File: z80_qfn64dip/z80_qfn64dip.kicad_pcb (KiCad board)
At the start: 2 copper layers, 62.8 x 23 mm, 28 parts, among them U1 Caravel_QFN, U2 Z80CPU, U3 AZ1117-3.3, U4 AP2112K-1.8, X1 10MHz

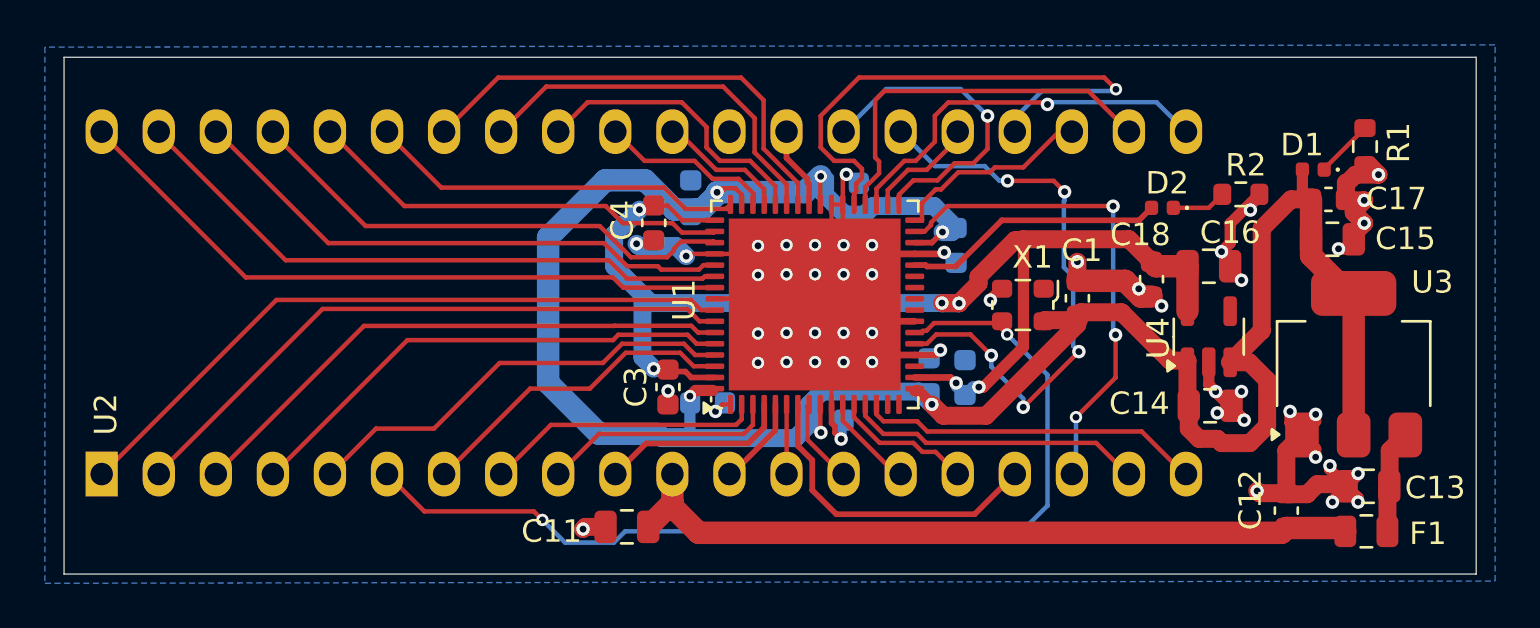
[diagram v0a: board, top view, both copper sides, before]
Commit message: add flash and move to 4 layers
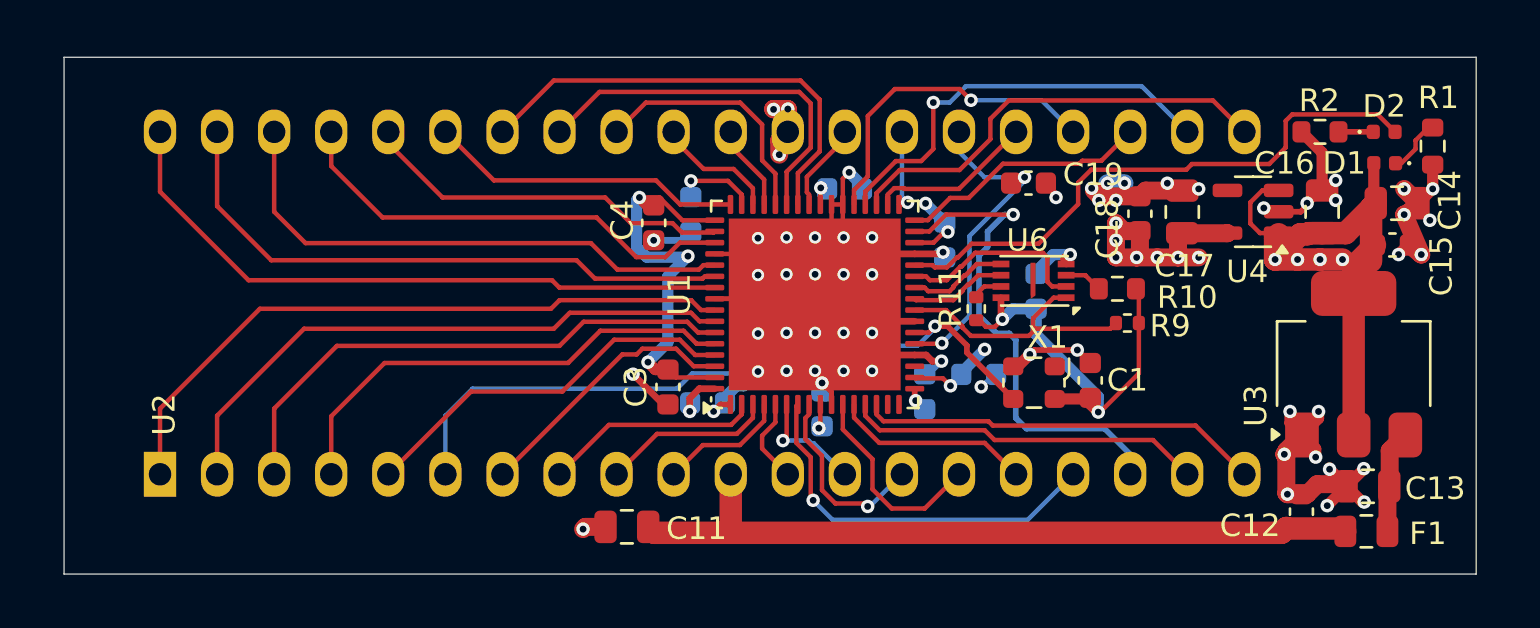
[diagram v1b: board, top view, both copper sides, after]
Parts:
- added C19: 1uF, Capacitor_SMD:C_0603_1608Metric, F.Cu at (157.5, 78.1)
- added C20: 100nF, Capacitor_SMD:C_0603_1608Metric, B.Cu at (157.9, 82.9)
- added R10: 10k, Resistor_SMD:R_0603_1608Metric, F.Cu at (161.5, 82.8)
- added R11: 10k, Resistor_SMD:R_0402_1005Metric, F.Cu at (155.2, 83.7)
- added R9: 10k, Resistor_SMD:R_0402_1005Metric, F.Cu at (161.9, 84.3)
- added U6: AT25EU0081A, KiCadModels:UDFN-8-1EP-2x3mm_P0.5mm_EP1.6x0.2mm, F.Cu at (157.7, 82.5)
- C14: value 10uF -> 22uF
- C15: value 22uF -> 100nF; footprint Capacitor_SMD:C_0805_2012Metric -> Capacitor_SMD:C_0603_1608Metric
- C17: value 100nF -> 10uF; footprint Capacitor_SMD:C_0603_1608Metric -> Capacitor_SMD:C_0805_2012Metric
- moved C14 12.3 mm to (173.9, 79.0)
- moved D2 10.4 mm to (173.4, 75.8), turned to 0 degrees
- moved C17 6.53 mm to (164.4, 79.4), turned to 90 degrees
- moved U4 5.90 mm to (167.5, 79.4), turned to 180 degrees
- moved C16 5.59 mm to (170.6, 79.4), turned to 90 degrees
- moved R2 4.49 mm to (170.5, 75.8), turned to 180 degrees
- moved C1 3.70 mm to (160.3, 86.9)
- moved X1 3.49 mm to (157.8, 87.0)
- moved D1 3.19 mm to (173.4, 77.2)
- moved R1 3.01 mm to (175.5, 76.5)
- moved C18 2.96 mm to (162.5, 79.5), turned to 90 degrees
- moved C15 2.68 mm to (173.7, 80.9)
- moved U2 2.60 mm to (118.9, 91.1)
- moved C8 0.75 mm to (142.5, 79.5), turned to -90 degrees
- moved C5 0.74 mm to (152.9, 87.4)
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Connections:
- C16 pad 1: +1V8 -> +3V3
- C17 pad 1: +3V3 -> +1V8
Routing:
- net +3V3: track 111.5 -> 57.8 mm, vias 6 -> 13
- net +1V8: track 54.9 -> 32.8 mm, vias 6 -> 12
- net gpio: track 11.6 -> 25.8 mm
- net osc_out: track 44.5 -> 32.1 mm, vias 2 -> 1
- net flash_csb: track 0.00 -> 12.1 mm
- net ~{SOC_RST}: track 26.2 -> 15.1 mm, vias 5 -> 2
- net /prj_io2: track 14.4 -> 3.67 mm
- net /prj_io6: track 25.1 -> 14.6 mm
- net flash_io1: track 0.00 -> 8.58 mm
- net /prj_io32: track 4.29 -> 9.16 mm
- net /prj_io31: track 3.84 -> 8.64 mm, vias 0 -> 1
- net flash_io0: track 0.00 -> 4.44 mm
- net flash_clk: track 0.00 -> 4.13 mm
- net /prj_io30: track 14.3 -> 17.4 mm, vias 0 -> 1
- net /prj_io26: track 10.2 -> 7.34 mm
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- added copper zone on In2.Cu, net +1V8
- added copper zone on In2.Cu, net +3V3
- added copper zone on In1.Cu, net GND
- added copper zone on In2.Cu, net GND
- removed copper zone on B.Cu, net GND
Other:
- copper layers 2 -> 4

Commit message: hand solder pads for bottom caps, minor tweaks to layout
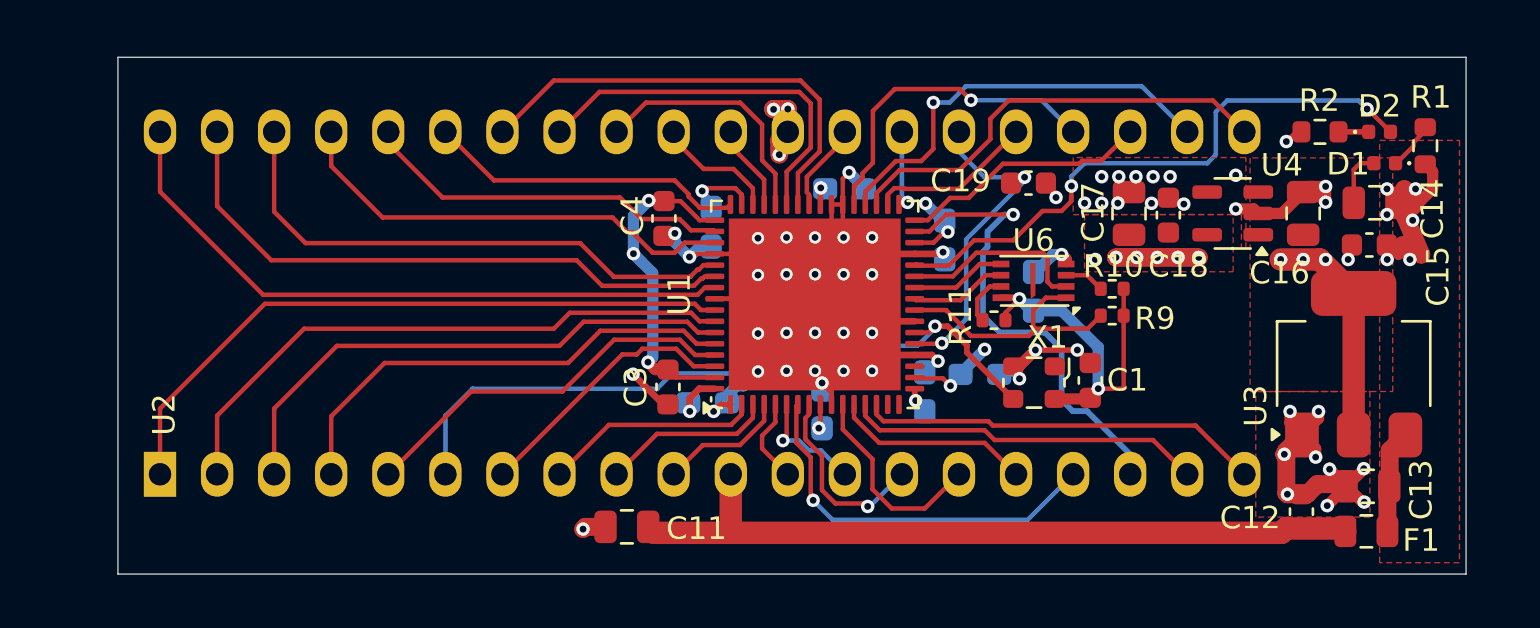
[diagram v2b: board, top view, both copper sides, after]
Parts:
- C10, C2, C20, C5, C6, C7, C8, C9: footprint Capacitor_SMD:C_0603_1608Metric -> Capacitor_SMD:C_0603_1608Metric_Pad1.08x0.95mm_HandSolder
- R10: footprint Resistor_SMD:R_0603_1608Metric -> Resistor_SMD:R_0402_1005Metric
- moved C17 2.37 mm to (162.0, 79.5)
- moved C18 1.27 mm to (163.8, 79.5)
- moved C8 1.07 mm to (143.4, 80.1)
- moved C15 1.03 mm to (172.7, 80.9)
- moved C14 0.98 mm to (172.9, 79.0)
- moved R11 0.94 mm to (156.0, 84.2), turned to 0 degrees
- moved U4 0.91 mm to (166.6, 79.5)
- moved C16 0.85 mm to (169.8, 79.5)
- moved R9 0.75 mm to (161.2, 84.0)
- moved C4 0.50 mm to (141.3, 79.7)
- moved R1 0.33 mm to (175.2, 76.4)
- moved R10 0.23 mm to (161.2, 82.8)
- moved D2 0.20 mm to (173.2, 75.8)
- moved C20 0.11 mm to (157.8, 82.9)
- moved C2 0.05 mm to (155.4, 86.6)
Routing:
- net +3V3: track 57.8 -> 40.5 mm
- net +1V8: track 32.8 -> 27.6 mm, vias 12 -> 11
- net GND: track 82.1 -> 79.4 mm, vias 62 -> 67
- net Net-(U6-~{HOLD}(IO_{3})): track 1.24 -> 2.32 mm
- net /prj_io0: track 22.3 -> 21.3 mm
- net gpio: track 25.8 -> 26.5 mm, vias 0 -> 2
- added copper zone on F.Cu, net +1V8
- added copper zone on F.Cu, net +3V3
- added copper zone on F.Cu, net GND
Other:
- board size 62.8 x 23 mm -> 60 x 23 mm

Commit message: jtag/spi connector
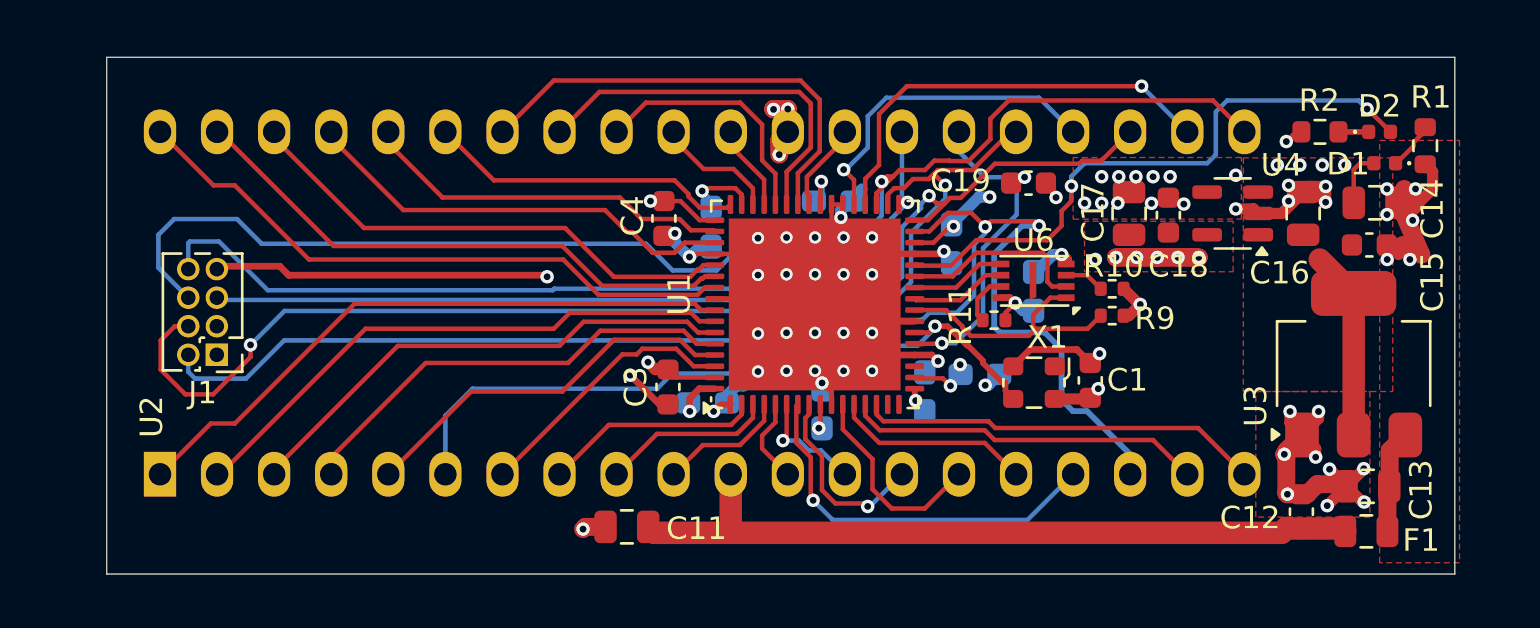
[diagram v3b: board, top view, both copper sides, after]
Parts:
- added J1: Conn_02x04_Odd_Even, Connector_PinHeader_1.27mm:PinHeader_2x04_P1.27mm_Vertical, F.Cu at (121.4, 85.7)
- moved C7 0.74 mm to (148.8, 78.9)
- moved C6 0.35 mm to (154.1, 80.8)
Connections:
- net /prj_io0 renamed HK_JTAG
- net /prj_io1 renamed HK_SDO
- net /prj_io2 renamed HK_SDI
- net /prj_io3 renamed HK_CSB
- net /prj_io4 renamed HK_SCK
- net /prj_io5 renamed ser_rx
- net /prj_io6 renamed ser_tx
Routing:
- net HK_CSB: track 7.34 -> 52.3 mm, vias 0 -> 2
- net HK_JTAG: track 21.3 -> 63.4 mm, vias 1 -> 2
- net HK_SCK: track 19.7 -> 59.8 mm, vias 0 -> 1
- net HK_SDI: track 3.67 -> 40.9 mm
- net HK_SDO: track 11.2 -> 47.1 mm, vias 0 -> 1
- net +1V8: track 27.6 -> 16.7 mm, vias 11 -> 10
- net +3V3: track 40.5 -> 46.8 mm, vias 13 -> 15
- net /prj_io17: track 27.2 -> 25.2 mm
- net /prj_io16: track 24.6 -> 22.7 mm
- net /prj_io19: track 29.7 -> 27.9 mm
- net /prj_io21: track 24.3 -> 22.7 mm
- net /prj_io18: track 29.4 -> 27.8 mm
- net /prj_io20: track 26.8 -> 25.3 mm
- net /prj_io22: track 21.5 -> 20.4 mm
- net GND: track 79.4 -> 80.3 mm, vias 67 -> 68
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
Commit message: remove crystal; testpoints connected directly to flash
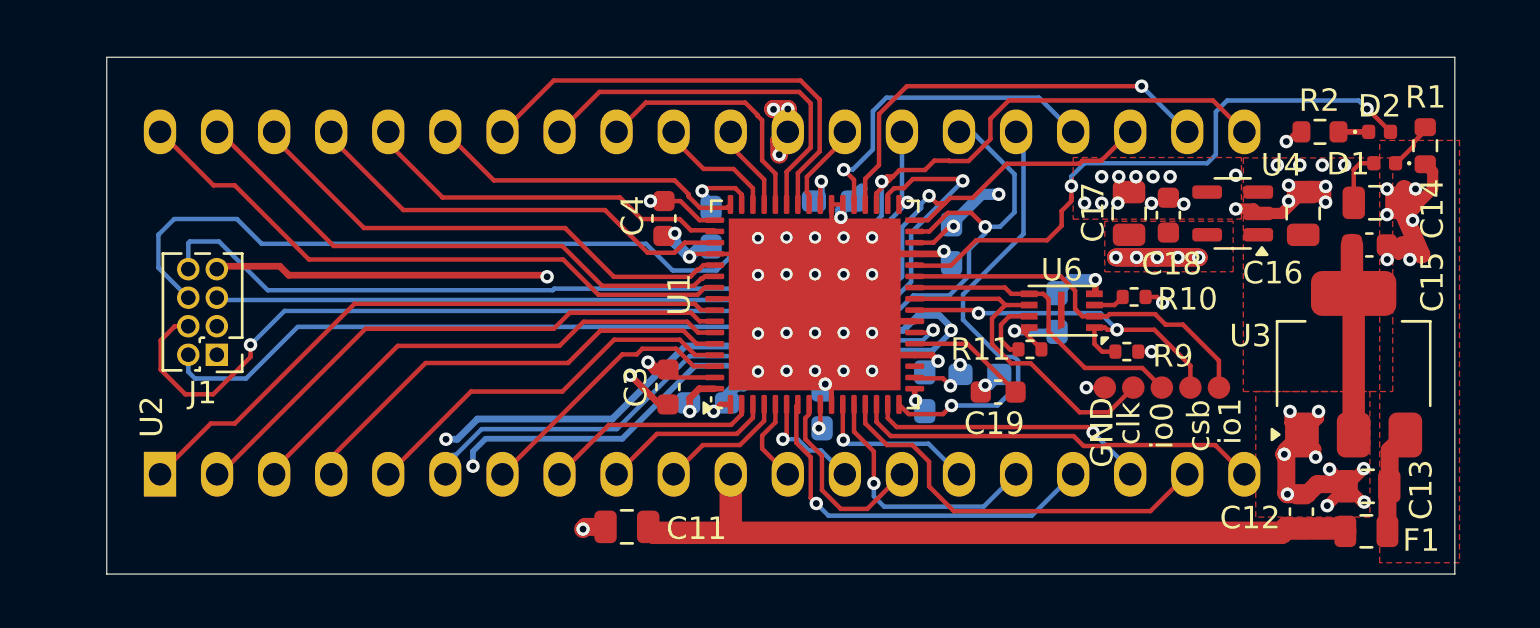
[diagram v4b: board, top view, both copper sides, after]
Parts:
- removed C1: 100nF, Capacitor_SMD:C_0603_1608Metric
- removed X1: 10MHz, Oscillator:Oscillator_SMD_ECS_2520MV-xxx-xx-4Pin_2.5x2.0mm
- added TP10: io0, TestPoint:TestPoint_Pad_D1.0mm, F.Cu at (163.5, 87.2)
- added TP11: clk, TestPoint:TestPoint_Pad_D1.0mm, F.Cu at (162.2, 87.2)
- added TP12: csb, TestPoint:TestPoint_Pad_D1.0mm, F.Cu at (164.7, 87.2)
- added TP13: GND, TestPoint:TestPoint_Pad_D1.0mm, F.Cu at (160.9, 87.2)
- added TP9: io1, TestPoint:TestPoint_Pad_D1.0mm, F.Cu at (166.0, 87.2)
- moved C19 9.40 mm to (156.2, 87.4), turned to 180 degrees
- moved R11 2.06 mm to (157.6, 85.5)
- moved U6 1.83 mm to (159.0, 83.8)
- moved R9 1.73 mm to (161.9, 85.6)
- moved C20 1.41 mm to (158.8, 83.9)
- moved R10 1.04 mm to (162.2, 83.2)
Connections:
- U2 pad 18: HK_JTAG -> /prj_io36
- U2 pad 25: HK_CSB -> /prj_io37
- U2 pad 26: ~{SOC_RST} -> HK_JTAG
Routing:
- net GND: track 80.3 -> 128.8 mm, vias 68 -> 70
- net /prj_io37: track 0.00 -> 19.9 mm, vias 0 -> 1
- net HK_JTAG: track 63.4 -> 50.3 mm, vias 2 -> 1
- net /prj_io36: track 0.00 -> 12.6 mm, vias 0 -> 1
- net flash_clk: track 4.10 -> 15.2 mm
- net ~{SOC_RST}: track 15.5 -> 5.38 mm, vias 2 -> 0
- net flash_io0: track 4.28 -> 13.7 mm
- net flash_io1: track 8.43 -> 16.8 mm
- net osc_out: track 32.2 -> 25.5 mm
- net flash_csb: track 11.7 -> 17.2 mm, vias 0 -> 2
- net HK_CSB: track 52.3 -> 48.6 mm
- net /prj_io33: track 8.84 -> 11.6 mm, vias 0 -> 1
- net /prj_io34: track 15.9 -> 18.1 mm
- net /prj_io32: track 9.16 -> 7.37 mm, vias 0 -> 1
- net Net-(U6-~{HOLD}(IO_{3})): track 2.32 -> 3.06 mm
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
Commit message: tweak connections due to changed caravel pinout
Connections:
- U2 pad 15: /prj_io32 -> /prj_io30
- U2 pad 17: /prj_io30 -> /prj_io32
- U2 pad 18: /prj_io36 -> /prj_io34
- U2 pad 19: /prj_io34 -> /prj_io35
- U2 pad 20: /prj_io35 -> /prj_io36
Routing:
- net /prj_io30: track 17.2 -> 12.1 mm, vias 1 -> 0
- net /prj_io36: track 12.6 -> 17.5 mm, vias 1 -> 0
- net /prj_io32: track 7.37 -> 12.3 mm
- net /prj_io34: track 18.1 -> 16.1 mm
- net /prj_io35: track 18.1 -> 16.5 mm

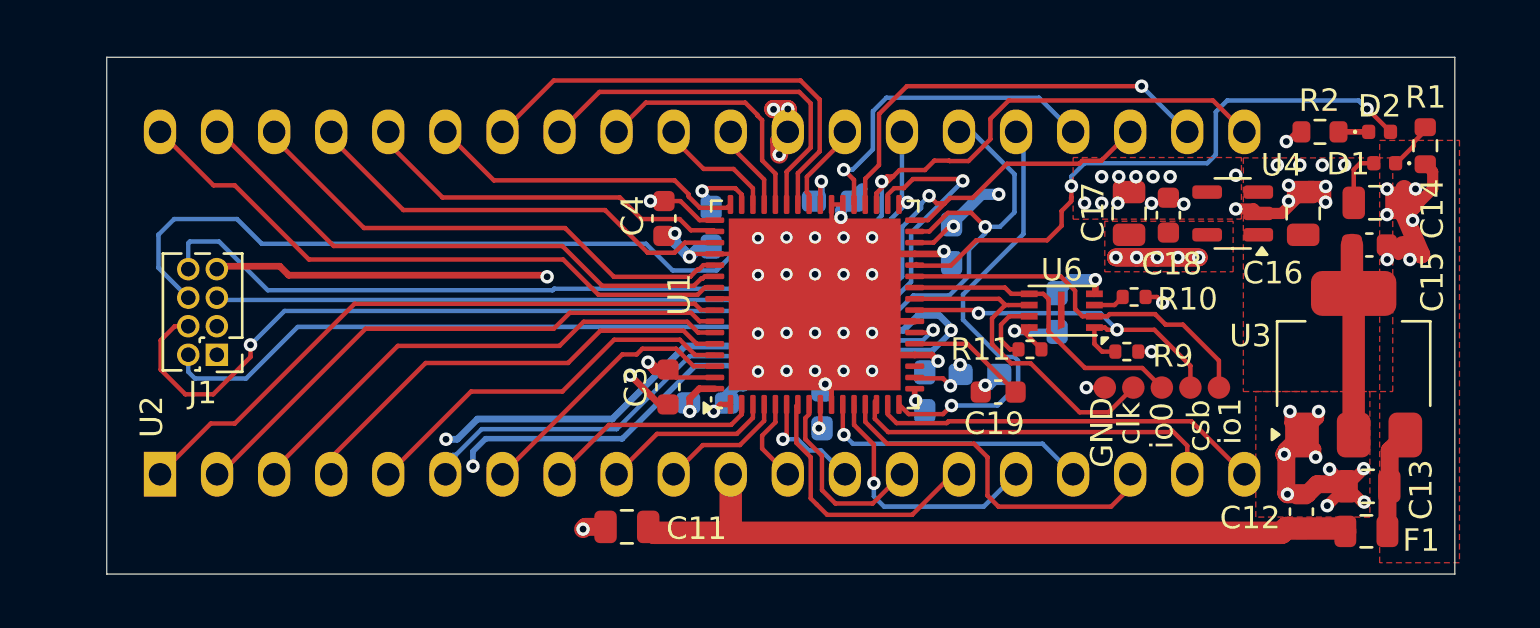
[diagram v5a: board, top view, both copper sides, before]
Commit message: layout tweaks, update to kicad 9
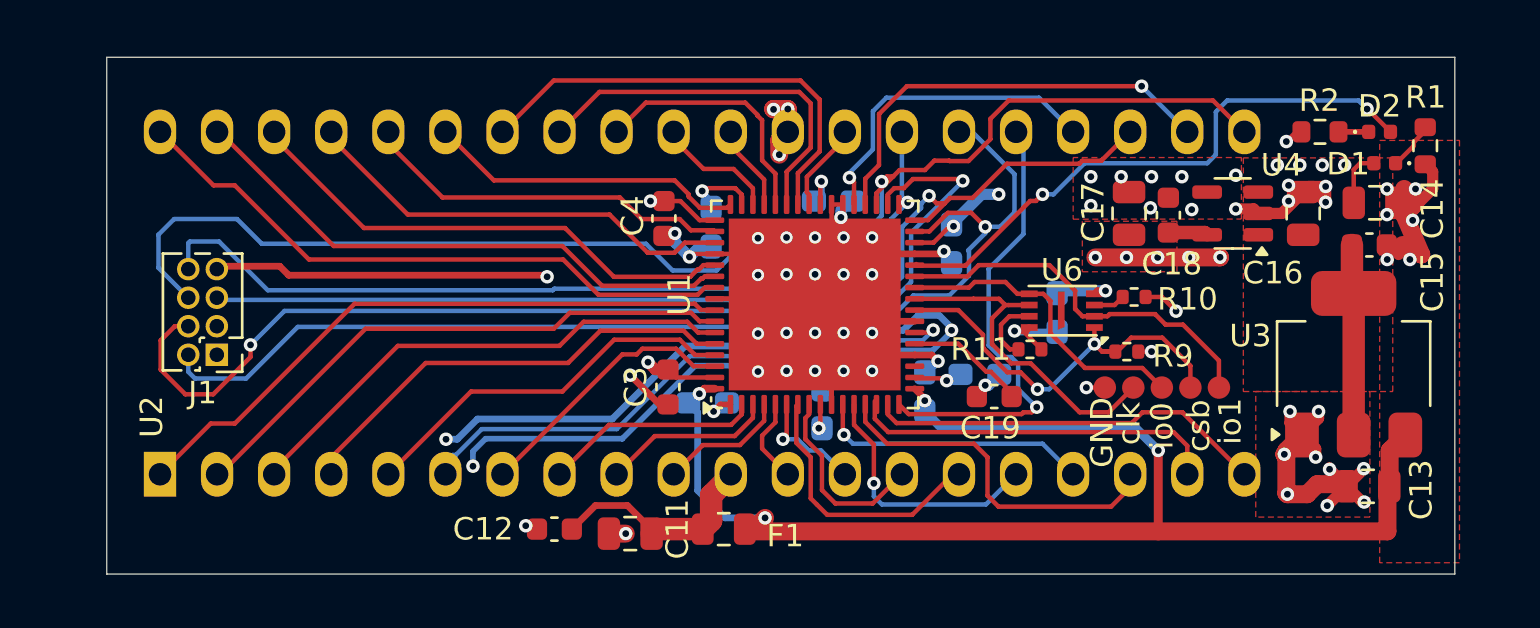
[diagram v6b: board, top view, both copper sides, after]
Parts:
- moved C12 33.3 mm to (136.4, 93.5), turned to 180 degrees
- moved F1 28.6 mm to (144.0, 93.5)
- moved C11 0.34 mm to (139.8, 93.7)
- moved C19 0.27 mm to (156.0, 87.6)
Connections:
- C10 pad 2: +3V3 -> +5V
- C5 pad 2: +3V3 -> +5V
- U1 pad 17: +3V3 -> +5V
- U1 pad 64: +3V3 -> +5V
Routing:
- net +5V: track 4.62 -> 59.7 mm, vias 0 -> 4
- net /VIN: track 33.9 -> 9.92 mm
- net +3V3: track 46.1 -> 43.5 mm, vias 15 -> 13
- net GND: track 128.8 -> 126.4 mm, vias 70 -> 67
- net gpio: track 26.9 -> 25.9 mm
- net flash_csb: track 17.2 -> 18.1 mm
- net /prj_io37: track 19.9 -> 20.7 mm
- net +1V8: track 16.7 -> 16.0 mm, vias 9 -> 8
